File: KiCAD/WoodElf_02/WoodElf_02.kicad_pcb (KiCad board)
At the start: 2 copper layers, 19.2 x 19.2 mm, 19 parts

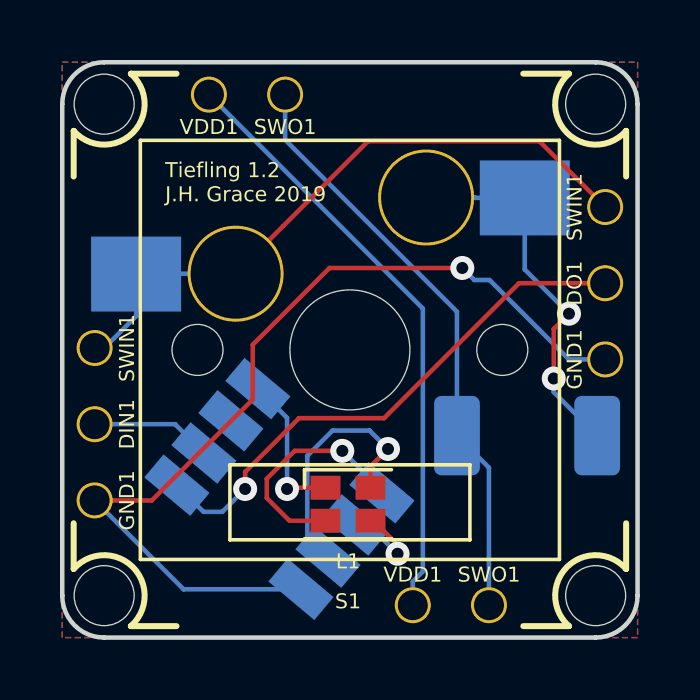
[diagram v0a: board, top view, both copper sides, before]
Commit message: rotated the ws2811 chip so that everything is at right angles
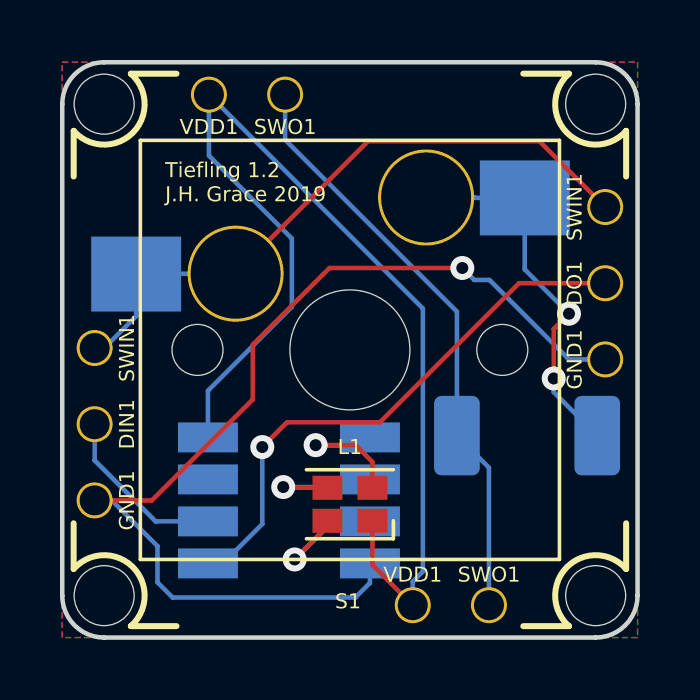
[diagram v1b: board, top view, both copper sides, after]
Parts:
- moved C1 0.50 mm to (138.6, 112.6), turned to 270 degrees
- moved L1 0.06 mm to (140.7, 112.8), turned to 180 degrees
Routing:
- net /USB: track 25.5 -> 37.3 mm, vias 1 -> 0
- net /GND: track 30.7 -> 34.6 mm
- net Net-(C1-Pad1): track 7.76 -> 4.90 mm
- net Net-(C1-Pad3): track 8.49 -> 5.96 mm
- net /DIN: track 4.04 -> 5.83 mm
- net Net-(C1-Pad2): track 3.35 -> 4.48 mm

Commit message: fixed up a via that was overlaping a silkscreen
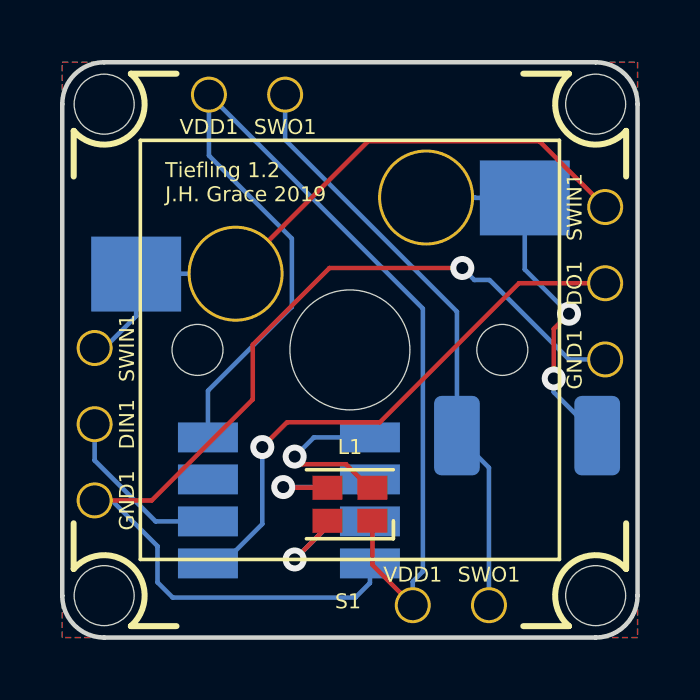
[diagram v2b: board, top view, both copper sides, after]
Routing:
- net Net-(C1-Pad1): track 4.90 -> 6.16 mm
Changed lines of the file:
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@@
     (thickness 1.6)
     (drawings 38)
-    (tracks 84)
+    (tracks 86)
     (zones 0)
     (modules 19)
@@
   (segment (start 139.9025 113.526) (end 139.9025 113.326) (width 0.1524) (layer F.Cu) (net 2))
   (segment (start 138.811 114.6175) (end 139.9025 113.526) (width 0.1524) (layer F.Cu) (net 2))
-  (segment (start 141.4025 112.226) (end 141.4025 111.367) (width 0.1524) (layer F.Cu) (net 3))
-  (via (at 139.5095 110.8075) (size 0.8) (drill 0.4) (layers F.Cu B.Cu) (net 3))
-  (segment (start 141.4025 111.367) (end 140.843 110.8075) (width 0.1524) (layer F.Cu) (net 3))
-  (segment (start 140.843 110.8075) (end 139.5095 110.8075) (width 0.1524) (layer F.Cu) (net 3))
   (segment (start 141.062 110.8075) (end 141.3205 110.549) (width 0.1524) (layer B.Cu) (net 3))
-  (segment (start 139.5095 110.8075) (end 141.062 110.8075) (width 0.1524) (layer B.Cu) (net 3))
+  (via (at 138.811 111.1885) (size 0.8) (drill 0.4) (layers F.Cu B.Cu) (net 3))
+  (segment (start 141.3205 110.549) (end 139.4505 110.549) (width 0.1524) (layer B.Cu) (net 3))
+  (segment (start 139.4505 110.549) (end 138.811 111.1885) (width 0.1524) (layer B.Cu) (net 3))
+  (segment (start 138.811 111.1885) (end 139.065 111.4425) (width 0.1524) (layer F.Cu) (net 3))
+  (segment (start 139.065 111.4425) (end 140.519 111.4425) (width 0.1524) (layer F.Cu) (net 3))
+  (segment (start 141.3025 112.226) (end 141.4025 112.226) (width 0.1524) (layer F.Cu) (net 3))
+  (segment (start 140.519 111.4425) (end 141.3025 112.226) (width 0.1524) (layer F.Cu) (net 3))
   (segment (start 142.748 115.356472) (end 142.748 116.1415) (width 0.1524) (layer B.Cu) (net 5))
   (segment (start 143.084822 115.01965) (end 142.748 115.356472) (width 0.1524) (layer B.Cu) (net 5))

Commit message: Cleaned up some more traces
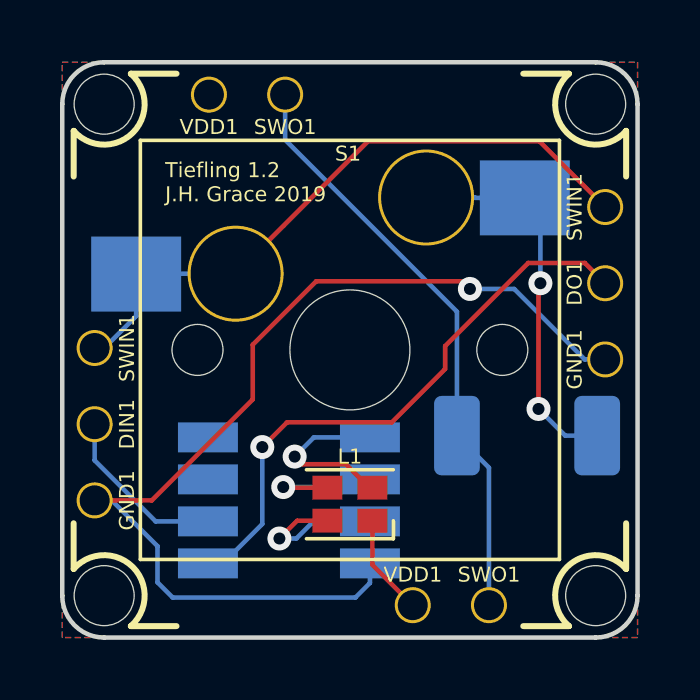
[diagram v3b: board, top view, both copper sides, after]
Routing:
- net /USB: track 37.3 -> 3.47 mm
- net /DO: track 18.6 -> 19.6 mm
- net Net-(C1-Pad3): track 5.96 -> 6.48 mm
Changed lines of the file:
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@@
     (thickness 1.6)
     (drawings 38)
-    (tracks 86)
+    (tracks 83)
     (zones 0)
     (modules 19)
@@
     (38 B.Mask user)
     (39 F.Mask user)
-    (40 Dwgs.User user)
+    (40 Dwgs.User user hide)
     (41 Cmts.User user)
     (42 Eco1.User user hide)
@@
     (descr "Cherry MX keyswitch, MX1A, 1.00u, PCB mount, http://cherryamericas.com/wp-content/uploads/2014/12/mx_cat.pdf")
     (tags "cherry mx keyswitch MX1A 1.00u PCB")
-    (fp_text reference S1 (at -2.6035 13.462) (layer F.SilkS)
+    (fp_text reference S1 (at -2.6035 -1.4605) (layer F.SilkS)
       (effects (font (size 0.5 0.5) (thickness 0.125)))
     )
@@
     (tags "LED Cree PLCC-4")
     (attr smd)
-    (fp_text reference L1 (at 0 1.905 180) (layer F.SilkS)
+    (fp_text reference L1 (at 0 1.5875 180) (layer F.SilkS)
       (effects (font (size 0.5 0.5) (thickness 0.125)))
     )
@@
   (segment (start 141.3205 113.349) (end 140.8205 113.349) (width 0.1524) (layer B.Cu) (net 2))
   (segment (start 140.819 113.3475) (end 140.1445 113.3475) (width 0.1524) (layer B.Cu) (net 2))
-  (via (at 138.811 114.6175) (size 0.8) (drill 0.4) (layers F.Cu B.Cu) (net 2))
   (segment (start 141.3205 113.349) (end 140.0795 113.349) (width 0.1524) (layer B.Cu) (net 2))
-  (segment (start 140.0795 113.349) (end 138.811 114.6175) (width 0.1524) (layer B.Cu) (net 2))
   (segment (start 139.9025 113.526) (end 139.9025 113.326) (width 0.1524) (layer F.Cu) (net 2))
-  (segment (start 138.811 114.6175) (end 139.9025 113.526) (width 0.1524) (layer F.Cu) (net 2))
+  (via (at 138.303 113.919) (size 0.8) (drill 0.4) (layers F.Cu B.Cu) (net 2))
+  (segment (start 139.9025 113.326) (end 138.896 113.326) (width 0.1524) (layer F.Cu) (net 2))
+  (segment (start 138.896 113.326) (end 138.303 113.919) (width 0.1524) (layer F.Cu) (net 2))
+  (segment (start 139.438685 113.349) (end 140.0795 113.349) (width 0.1524) (layer B.Cu) (net 2))
+  (segment (start 138.868685 113.919) (end 139.438685 113.349) (width 0.1524) (layer B.Cu) (net 2))
+  (segment (start 138.303 113.919) (end 138.868685 113.919) (width 0.1524) (layer B.Cu) (net 2))
   (segment (start 141.062 110.8075) (end 141.3205 110.549) (width 0.1524) (layer B.Cu) (net 3))
   (via (at 138.811 111.1885) (size 0.8) (drill 0.4) (layers F.Cu B.Cu) (net 3))
@@
   (segment (start 141.3025 112.226) (end 141.4025 112.226) (width 0.1524) (layer F.Cu) (net 3))
   (segment (start 140.519 111.4425) (end 141.3025 112.226) (width 0.1524) (layer F.Cu) (net 3))
-  (segment (start 142.748 115.356472) (end 142.748 116.1415) (width 0.1524) (layer B.Cu) (net 5))
-  (segment (start 143.084822 115.01965) (end 142.748 115.356472) (width 0.1524) (layer B.Cu) (net 5))
-  (segment (start 143.084822 106.254822) (end 143.084822 115.01965) (width 0.1524) (layer B.Cu) (net 5))
   (segment (start 141.4025 114.796) (end 142.748 116.1415) (width 0.1524) (layer F.Cu) (net 5))
   (segment (start 141.4025 113.326) (end 141.4025 114.796) (width 0.1524) (layer F.Cu) (net 5))
-  (segment (start 135.9535 99.1235) (end 143.084822 106.254822) (width 0.1524) (layer B.Cu) (net 5))
-  (segment (start 138.718701 106.197521) (end 138.718701 103.920701) (width 0.1524) (layer B.Cu) (net 5))
-  (segment (start 135.9205 110.549) (end 135.9205 108.995722) (width 0.1524) (layer B.Cu) (net 5))
-  (segment (start 135.9205 108.995722) (end 138.718701 106.197521) (width 0.1524) (layer B.Cu) (net 5))
-  (segment (start 135.9535 101.1555) (end 135.9535 99.1235) (width 0.1524) (layer B.Cu) (net 5))
-  (segment (start 138.718701 103.920701) (end 135.9535 101.1555) (width 0.1524) (layer B.Cu) (net 5))
   (segment (start 144.8167 102.5525) (end 143.1925 102.5525) (width 0.1524) (layer B.Cu) (net 6))
   (segment (start 144.8294 102.5652) (end 144.8167 102.5525) (width 0.1524) (layer B.Cu) (net 6))
   (segment (start 146.4818 102.5652) (end 144.8294 102.5652) (width 0.1524) (layer B.Cu) (net 6))
-  (via (at 147.447 108.585) (size 0.8) (drill 0.4) (layers F.Cu B.Cu) (net 6))
-  (segment (start 148.8955 110.49) (end 147.447 109.0415) (width 0.1524) (layer B.Cu) (net 6))
-  (segment (start 147.447 109.0415) (end 147.447 108.585) (width 0.1524) (layer B.Cu) (net 6))
-  (via (at 147.955 106.426) (size 0.8) (drill 0.4) (layers F.Cu B.Cu) (net 6))
-  (segment (start 147.447 108.585) (end 147.447 106.934) (width 0.1524) (layer F.Cu) (net 6))
-  (segment (start 147.447 106.934) (end 147.955 106.426) (width 0.1524) (layer F.Cu) (net 6))
-  (segment (start 146.4818 104.9528) (end 146.4818 102.5652) (width 0.1524) (layer B.Cu) (net 6))
-  (segment (start 147.955 106.426) (end 146.4818 104.9528) (width 0.1524) (layer B.Cu) (net 6))
-  (via (at 144.399 104.902) (size 0.8) (drill 0.4) (layers F.Cu B.Cu) (net 7))
-  (segment (start 144.798999 105.301999) (end 144.399 104.902) (width 0.1524) (layer B.Cu) (net 7))
-  (segment (start 145.306999 105.301999) (end 144.798999 105.301999) (width 0.1524) (layer B.Cu) (net 7))
-  (segment (start 149.1615 107.95) (end 147.955 107.95) (width 0.1524) (layer B.Cu) (net 7))
-  (segment (start 147.955 107.95) (end 145.306999 105.301999) (width 0.1524) (layer B.Cu) (net 7))
+  (via (at 146.939 109.601) (size 0.8) (drill 0.4) (layers F.Cu B.Cu) (net 6))
+  (segment (start 148.8955 110.49) (end 147.828 110.49) (width 0.1524) (layer B.Cu) (net 6))
+  (segment (start 147.828 110.49) (end 146.939 109.601) (width 0.1524) (layer B.Cu) (net 6))
+  (via (at 147.0025 105.41) (size 0.8) (drill 0.4) (layers F.Cu B.Cu) (net 6))
+  (segment (start 146.939 109.601) (end 146.939 105.4735) (width 0.1524) (layer F.Cu) (net 6))
+  (segment (start 146.939 105.4735) (end 147.0025 105.41) (width 0.1524) (layer F.Cu) (net 6))
+  (segment (start 147.0025 103.0859) (end 146.4818 102.5652) (width 0.1524) (layer B.Cu) (net 6))
+  (segment (start 147.0025 105.41) (end 147.0025 103.0859) (width 0.1524) (layer B.Cu) (net 6))
   (segment (start 134.0485 112.649) (end 132.1435 112.649) (width 0.1524) (layer F.Cu) (net 7))
   (segment (start 137.414 109.2835) (end 134.0485 112.649) (width 0.1524) (layer F.Cu) (net 7))
   (segment (start 137.414 107.457778) (end 137.414 109.2835) (width 0.1524) (layer F.Cu) (net 7))
-  (segment (start 144.399 104.902) (end 139.969778 104.902) (width 0.1524) (layer F.Cu) (net 7))
-  (segment (start 139.969778 104.902) (end 137.414 107.457778) (width 0.1524) (layer F.Cu) (net 7))
   (segment (start 132.1435 112.649) (end 132.715 112.649) (width 0.1524) (layer B.Cu) (net 7))
   (segment (start 132.715 112.649) (end 134.239 114.173) (width 0.1524) (layer B.Cu) (net 7))
@@
   (segment (start 141.3205 115.4014) (end 140.8344 115.8875) (width 0.1524) (layer B.Cu) (net 7))
   (segment (start 141.3205 114.749) (end 141.3205 115.4014) (width 0.1524) (layer B.Cu) (net 7))
+  (via (at 144.653 105.6005) (size 0.8) (drill 0.4) (layers F.Cu B.Cu) (net 7))
+  (segment (start 144.399 105.3465) (end 144.653 105.6005) (width 0.1524) (layer F.Cu) (net 7))
+  (segment (start 137.414 107.457778) (end 139.525278 105.3465) (width 0.1524) (layer F.Cu) (net 7))
+  (segment (start 139.525278 105.3465) (end 144.399 105.3465) (width 0.1524) (layer F.Cu) (net 7))
+  (segment (start 148.478222 107.95) (end 149.1615 107.95) (width 0.1524) (layer B.Cu) (net 7))
+  (segment (start 146.128722 105.6005) (end 148.478222 107.95) (width 0.1524) (layer B.Cu) (net 7))
+  (segment (start 144.653 105.6005) (end 146.128722 105.6005) (width 0.1524) (layer B.Cu) (net 7))
   (segment (start 132.1435 111.3155) (end 132.1435 110.109) (width 0.1524) (layer B.Cu) (net 8))
   (segment (start 135.920501 113.349) (end 134.177 113.349) (width 0.1524) (layer B.Cu) (net 8))
@@
   (segment (start 135.9205 114.749) (end 136.4205 114.749) (width 0.1524) (layer B.Cu) (net 9))
   (segment (start 136.4205 114.749) (end 137.7315 113.438) (width 0.1524) (layer B.Cu) (net 9))
-  (segment (start 146.288222 105.41) (end 149.1615 105.41) (width 0.1524) (layer F.Cu) (net 9))
-  (segment (start 141.652722 110.0455) (end 146.288222 105.41) (width 0.1524) (layer F.Cu) (net 9))
-  (segment (start 137.7315 110.871) (end 138.557 110.0455) (width 0.1524) (layer F.Cu) (net 9))
-  (segment (start 138.557 110.0455) (end 141.652722 110.0455) (width 0.1524) (layer F.Cu) (net 9))
+  (segment (start 148.485299 104.733799) (end 146.599201 104.733799) (width 0.1524) (layer F.Cu) (net 9))
+  (segment (start 149.1615 105.41) (end 148.485299 104.733799) (width 0.1524) (layer F.Cu) (net 9))
+  (segment (start 138.557 110.0455) (end 137.7315 110.871) (width 0.1524) (layer F.Cu) (net 9))
+  (segment (start 146.599201 104.733799) (end 143.8275 107.5055) (width 0.1524) (layer F.Cu) (net 9))
+  (segment (start 143.8275 107.5055) (end 143.8275 108.2675) (width 0.1524) (layer F.Cu) (net 9))
+  (segment (start 143.8275 108.2675) (end 142.0495 110.0455) (width 0.1524) (layer F.Cu) (net 9))
+  (segment (start 142.0495 110.0455) (end 138.557 110.0455) (width 0.1524) (layer F.Cu) (net 9))
   (segment (start 145.288 111.5575) (end 144.2205 110.49) (width 0.1524) (layer B.Cu) (net 10))
   (segment (start 144.2205 110.49) (end 144.2205 106.357278) (width 0.1524) (layer B.Cu) (net 10))

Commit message: cleaned up some more traces, updated the silkscreen credit
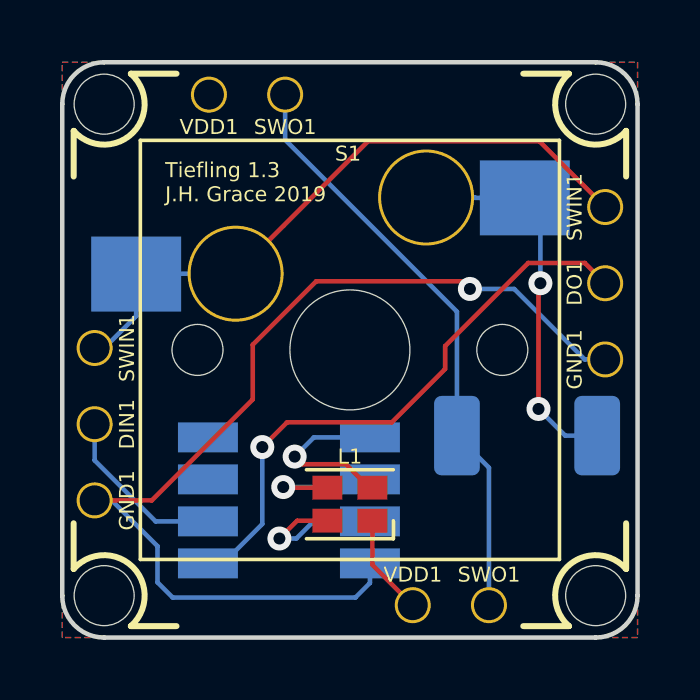
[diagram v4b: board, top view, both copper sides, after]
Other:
- board text added: "Tiefling 1.3 J.H. Grace 2019"
- board text removed: "Tiefling 1.2 J.H. Grace 2019"
